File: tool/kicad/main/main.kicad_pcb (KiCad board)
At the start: 2 copper layers, 71.9 x 39.3 mm, 91 parts, among them J1 MICRO-USB-AB, K1 CONN_3, P10 TEST_POINT, P27 TEST_POINT, P28 TEST_POINT, P29 TEST_POINT, P30 CONN_3X2, P31 CONN_7, P35 CONN_6, P37 TEST_POINT, P38 TEST_POINT, P5 CONN_6, U1 SN74LVC2T45, U2 ST-USBLC6-2, U3 EFM32GG332, U4 YM2413, X1 48Mhz, X2 CRYSTAL

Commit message: more main board work
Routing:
- net /XIN': track 0.00 -> 13.7 mm
- net /XOUT': track 0.00 -> 9.36 mm
- net Net-(C16-Pad1): track 0.00 -> 9.02 mm
- net Net-(C15-Pad1): track 0.00 -> 8.67 mm
- net +5V: track 19.3 -> 26.8 mm, vias 0 -> 1
- net /XIN: track 0.00 -> 7.30 mm
- net /XOUT: track 0.00 -> 6.58 mm
- net GND: track 56.6 -> 61.6 mm, vias 29 -> 33
- net /XIN3V3: track 0.00 -> 3.33 mm
- net /XOUT3V3: track 0.00 -> 3.33 mm
- net Net-(JP3-Pad2): track 0.00 -> 1.94 mm
- net Net-(JP2-Pad2): track 0.00 -> 1.94 mm
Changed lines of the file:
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@@
   (general
     (links 190)
-    (no_connects 43)
+    (no_connects 23)
     (area 84.149999 73.549999 156.150001 112.950001)
     (thickness 1.6)
     (drawings 14)
-    (tracks 478)
+    (tracks 531)
     (zones 0)
     (modules 91)
@@
   (segment (start 106.5 88) (end 106 88) (width 0.3048) (layer F.Cu) (net 2))
   (segment (start 106.75 88.25) (end 106.5 88) (width 0.3048) (layer F.Cu) (net 2))
+  (segment (start 120.45 97.775) (end 123.095 97.775) (width 0.3048) (layer F.Cu) (net 3) (status 400000))
+  (via (at 125.69 94.02) (size 0.635) (layers F.Cu B.Cu) (net 3))
+  (segment (start 125.28 94.43) (end 125.69 94.02) (width 0.3048) (layer F.Cu) (net 3))
+  (segment (start 125.28 95.59) (end 125.28 94.43) (width 0.3048) (layer F.Cu) (net 3))
+  (segment (start 123.095 97.775) (end 125.28 95.59) (width 0.3048) (layer F.Cu) (net 3))
   (segment (start 120.2 76.1) (end 120.2 75.4) (width 0.3048) (layer F.Cu) (net 3))
   (segment (start 120.2 75.4) (end 120.8 74.8) (width 0.3048) (layer F.Cu) (net 3))
@@
   (segment (start 91.1 100.2) (end 92.8 100.2) (width 0.2032) (layer F.Cu) (net 51))
   (segment (start 90.7 99.8) (end 91.1 100.2) (width 0.2032) (layer F.Cu) (net 51))
+  (segment (start 126.5 95.4) (end 126.47 95.4) (width 0.2032) (layer F.Cu) (net 52) (status C00000))
+  (segment (start 126.47 95.4) (end 123.445 98.425) (width 0.2032) (layer F.Cu) (net 52) (status 400000))
+  (segment (start 123.445 98.425) (end 120.45 98.425) (width 0.2032) (layer F.Cu) (net 52) (status 800000))
+  (segment (start 130.2 96.75) (end 133.11 96.75) (width 0.2032) (layer F.Cu) (net 53) (status C00000))
+  (segment (start 133.11 96.75) (end 133.34 96.52) (width 0.2032) (layer F.Cu) (net 53) (status C00000))
+  (segment (start 138.8 103) (end 138.8 98.97) (width 0.2032) (layer F.Cu) (net 53) (status 400000))
+  (segment (start 136.35 96.52) (end 133.34 96.52) (width 0.2032) (layer F.Cu) (net 53) (status 800000))
+  (segment (start 138.8 98.97) (end 136.35 96.52) (width 0.2032) (layer F.Cu) (net 53))
+  (segment (start 117.05 98.425) (end 115.475 98.425) (width 0.2032) (layer F.Cu) (net 54) (status 400000))
+  (segment (start 115.4 98.5) (end 113.75 98.5) (width 0.2032) (layer F.Cu) (net 54) (status 800000))
+  (segment (start 115.475 98.425) (end 115.4 98.5) (width 0.2032) (layer F.Cu) (net 54))
+  (segment (start 126.5 100.35) (end 124.85 100.35) (width 0.2032) (layer F.Cu) (net 55) (status 400000))
+  (segment (start 123.575 99.075) (end 120.45 99.075) (width 0.2032) (layer F.Cu) (net 55) (status 800000))
+  (segment (start 124.85 100.35) (end 123.575 99.075) (width 0.2032) (layer F.Cu) (net 55))
+  (segment (start 130.2 99) (end 133.28 99) (width 0.2032) (layer F.Cu) (net 56) (status C00000))
+  (segment (start 133.28 99) (end 133.34 99.06) (width 0.2032) (layer F.Cu) (net 56) (status C00000))
+  (segment (start 134.55 103) (end 134.55 102.11) (width 0.2032) (layer F.Cu) (net 56) (status 400000))
+  (segment (start 133.59 101.15) (end 132.2 101.15) (width 0.2032) (layer F.Cu) (net 56) (status 800000))
+  (segment (start 134.55 102.11) (end 133.59 101.15) (width 0.2032) (layer F.Cu) (net 56))
+  (segment (start 133.34 99.06) (end 133.34 100.01) (width 0.2032) (layer F.Cu) (net 56) (status 400000))
+  (segment (start 133.34 100.01) (end 132.2 101.15) (width 0.2032) (layer F.Cu) (net 56) (status 800000))
+  (segment (start 117.05 99.075) (end 113.825 99.075) (width 0.2032) (layer F.Cu) (net 57) (status C00000))
+  (segment (start 113.825 99.075) (end 113.75 99) (width 0.2032) (layer F.Cu) (net 57) (status C00000))
   (segment (start 107.525 84.675) (end 105.875 84.675) (width 0.2032) (layer F.Cu) (net 58))
   (segment (start 105.875 84.675) (end 105.85 84.65) (width 0.2032) (layer F.Cu) (net 58))
@@
   (segment (start 140.96 96.52) (end 143.73 96.52) (width 0.2032) (layer F.Cu) (net 67))
   (segment (start 143.73 96.52) (end 143.8 96.45) (width 0.2032) (layer F.Cu) (net 67))
+  (segment (start 117.05 99.725) (end 118.335 99.725) (width 0.3048) (layer F.Cu) (net 68) (status 400000))
+  (via (at 118.34 99.72) (size 0.635) (layers F.Cu B.Cu) (net 68))
+  (segment (start 118.335 99.725) (end 118.34 99.72) (width 0.3048) (layer F.Cu) (net 68))
+  (segment (start 144.75 108.6) (end 144.75 109.55) (width 0.3048) (layer F.Cu) (net 68) (status 400000))
+  (via (at 144.83 109.63) (size 0.635) (layers F.Cu B.Cu) (net 68))
+  (segment (start 144.75 109.55) (end 144.83 109.63) (width 0.3048) (layer F.Cu) (net 68))
+  (segment (start 130.75 108.6) (end 130.75 109.59) (width 0.3048) (layer F.Cu) (net 68) (status 400000))
+  (via (at 130.66 109.68) (size 0.635) (layers F.Cu B.Cu) (net 68))
+  (segment (start 130.75 109.59) (end 130.66 109.68) (width 0.3048) (layer F.Cu) (net 68))
+  (segment (start 132.2 103.05) (end 132.2 104.35) (width 0.3048) (layer F.Cu) (net 68) (status 400000))
+  (via (at 132.03 104.52) (size 0.635) (layers F.Cu B.Cu) (net 68))
+  (segment (start 132.2 104.35) (end 132.03 104.52) (width 0.3048) (layer F.Cu) (net 68))
   (segment (start 147.25 88.6) (end 148.26 88.6) (width 0.3048) (layer F.Cu) (net 68))
   (via (at 148.28 88.62) (size 0.635) (layers F.Cu B.Cu) (net 68))
@@
   (segment (start 93.5 98.5) (end 93.1 98.1) (width 0.3048) (layer F.Cu) (net 68))
   (segment (start 93.1 96.05) (end 93.45 95.7) (width 0.3048) (layer F.Cu) (net 68))
+  (segment (start 144.75 106.9) (end 140.39 106.9) (width 0.2032) (layer F.Cu) (net 69) (status C00000))
+  (segment (start 140.39 106.9) (end 140.29 107) (width 0.2032) (layer F.Cu) (net 69) (status C00000))
+  (segment (start 140.29 107) (end 140.29 103.41) (width 0.2032) (layer F.Cu) (net 69) (status C00000))
+  (segment (start 140.29 103.41) (end 140.7 103) (width 0.2032) (layer F.Cu) (net 69) (status C00000))
+  (segment (start 135.21 107) (end 130.85 107) (width 0.2032) (layer F.Cu) (net 70) (status C00000))
+  (segment (start 130.85 107) (end 130.75 106.9) (width 0.2032) (layer F.Cu) (net 70) (status C00000))
+  (segment (start 135.21 107) (end 135.21 106.85) (width 0.2032) (layer F.Cu) (net 70) (status C00000))
+  (segment (start 135.21 106.85) (end 136.45 105.61) (width 0.2032) (layer F.Cu) (net 70) (status 400000))
+  (segment (start 136.45 105.61) (end 136.45 103) (width 0.2032) (layer F.Cu) (net 70) (status 800000))
   (segment (start 128.35 76) (end 130.65 76) (width 0.2032) (layer F.Cu) (net 71))
   (segment (start 86.6 109.45) (end 86.6 107.65) (width 0.2032) (layer F.Cu) (net 72))
@@
   (segment (start 110.4 109.35) (end 110.4 107.8) (width 0.2032) (layer F.Cu) (net 80))
   (segment (start 113.4 109.35) (end 113.4 107.8) (width 0.2032) (layer F.Cu) (net 81))
+  (segment (start 128.3 96.75) (end 126.85 96.75) (width 0.2032) (layer F.Cu) (net 83) (status C00000))
+  (segment (start 126.85 96.75) (end 126.5 97.1) (width 0.2032) (layer F.Cu) (net 83) (status C00000))
+  (segment (start 128.3 99) (end 126.85 99) (width 0.2032) (layer F.Cu) (net 84) (status C00000))
+  (segment (start 126.85 99) (end 126.5 98.65) (width 0.2032) (layer F.Cu) (net 84) (status C00000))
   (segment (start 103.85 84.65) (end 103.85 83.55) (width 0.2032) (layer F.Cu) (net 85))
   (segment (start 103.85 83.55) (end 102.9 82.6) (width 0.2032) (layer F.Cu) (net 85))

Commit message: main finish rough layout
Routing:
- net /MIDI_IN: track 0.00 -> 83.4 mm, vias 0 -> 1
- net /~IC: track 1.67 -> 64.8 mm, vias 0 -> 2
- net +5V: track 26.8 -> 89.7 mm, vias 1 -> 5
- net /MO_SAMPLE: track 11.5 -> 72.6 mm, vias 0 -> 2
- net /~CS: track 1.65 -> 60.9 mm, vias 0 -> 2
- net /RO_SAMPLE: track 10.7 -> 69.4 mm, vias 0 -> 2
- net /~WE: track 1.67 -> 59.9 mm, vias 0 -> 2
- net /A0: track 0.00 -> 53.3 mm, vias 0 -> 2
- net +3.3V: track 107.0 -> 159.5 mm, vias 6 -> 14
- net /LED0: track 0.00 -> 33.0 mm, vias 0 -> 2
- net /LED1: track 0.00 -> 29.9 mm, vias 0 -> 2
- net /SWD: track 0.00 -> 29.4 mm, vias 0 -> 1
- net /SWO: track 0.00 -> 27.0 mm, vias 0 -> 1
- net /LED2: track 0.00 -> 26.8 mm, vias 0 -> 2
- net /LED4: track 0.00 -> 26.5 mm, vias 0 -> 2
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
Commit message: updated main board
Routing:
- net GND: track 67.8 -> 67.1 mm
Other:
- board text added: "MIDI"
- board text added: "MO"
- board text added: "MOS"
- board text added: "RO"
- board text added: "ROS"

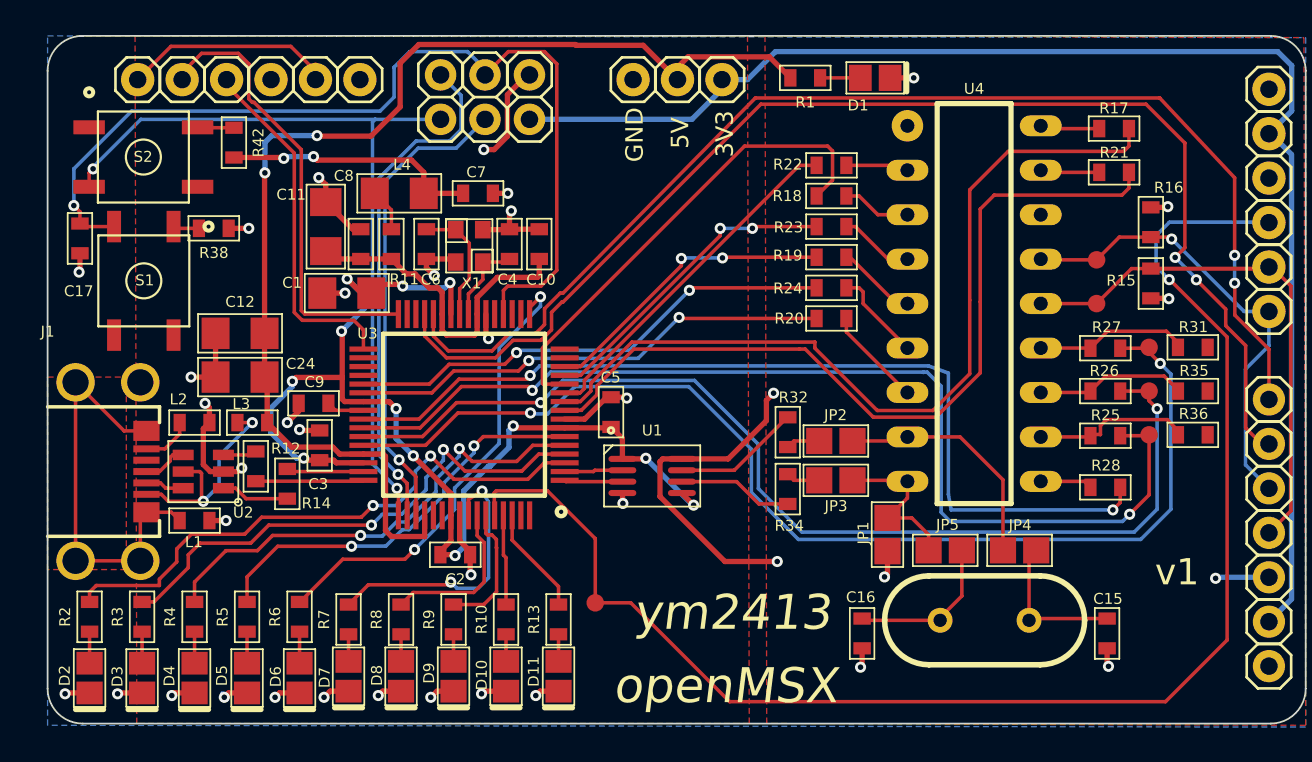
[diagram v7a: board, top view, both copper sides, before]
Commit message: fix main USB connector
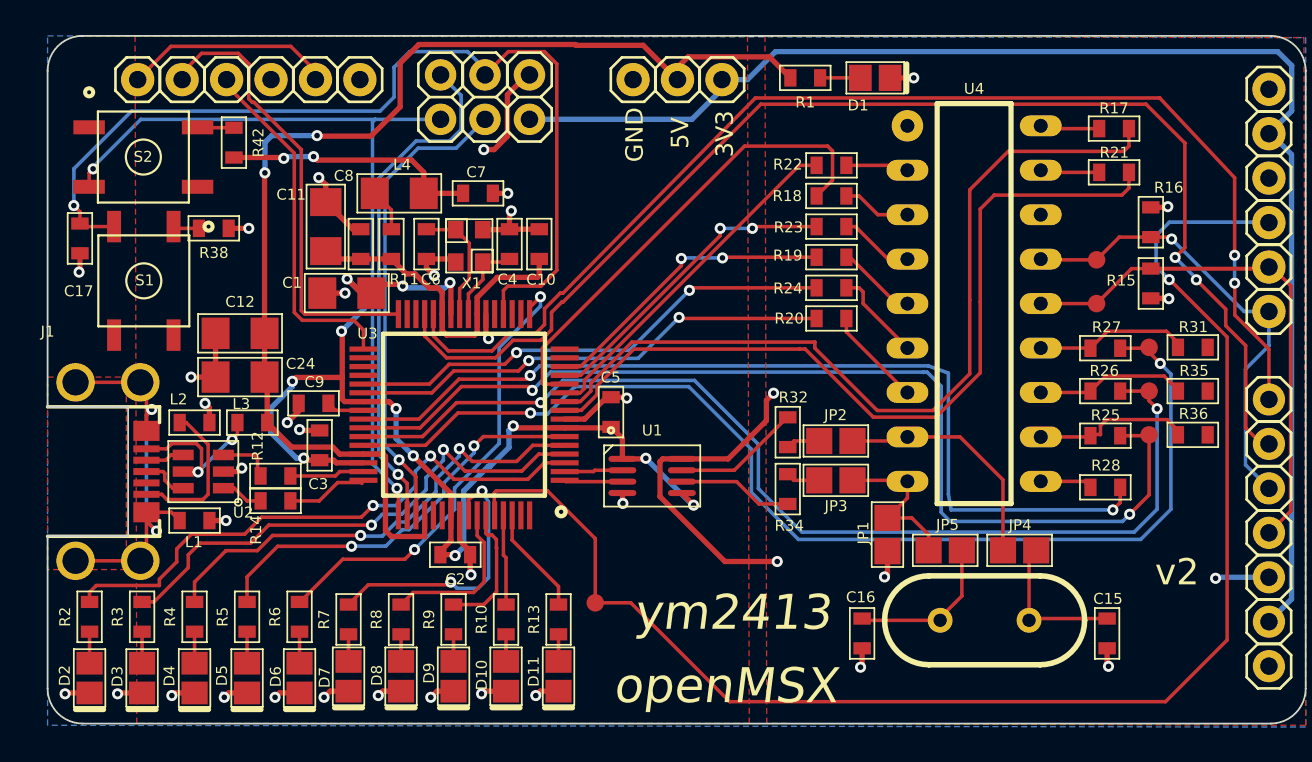
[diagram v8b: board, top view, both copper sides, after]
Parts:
- moved R12 1.25 mm to (97.2, 98.8), turned to 0 degrees
- moved R14 1.19 mm to (97.2, 100.2), turned to 0 degrees
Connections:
- J1 pad 11: (no net) -> /GI_2
- R12 pad 1: /D+B -> /D-B
- R12 pad 2: /D+ -> /D-
- R14 pad 1: /D-B -> /D+B
- R14 pad 2: /D- -> /D+
- U2 pad 1: /D-B -> /D+B
- U2 pad 3: /D+B -> /D-B
- U2 pad 4: /D+_IN -> /D-_IN
- U2 pad 6: /D-_IN -> /D+_IN
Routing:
- net /G_I1: track 2.90 -> 8.77 mm
- net GND: track 67.1 -> 63.2 mm
- net /VBUS_IN: track 12.7 -> 10.4 mm
- net /GI_2: track 24.1 -> 25.8 mm, vias 0 -> 2
- net /D+: track 6.17 -> 4.63 mm
- net /D-B: track 3.90 -> 3.12 mm
- net /D-_IN: track 2.22 -> 2.82 mm
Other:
- outline, holes or cut-outs redrawn
- board text added: "v2"
- board text removed: "v1"
